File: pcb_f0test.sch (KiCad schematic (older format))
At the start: 36 parts, among them P2 CONN_01X02, P6 CONN_02X05, U1 STM32F042GxU, U2 LP2985LV

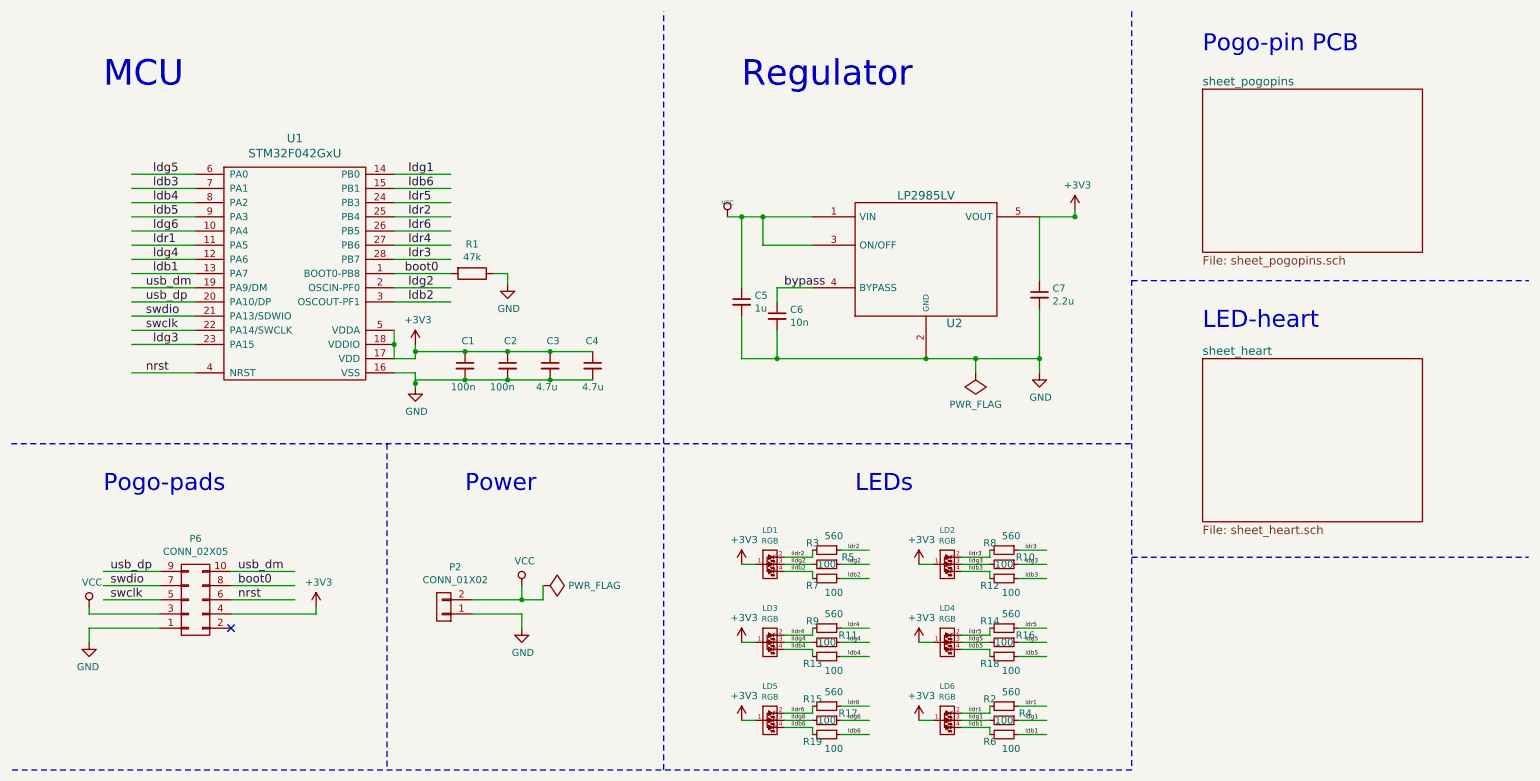
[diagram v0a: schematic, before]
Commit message: Change RGB LED footprint to match new batch of cheap 0603.
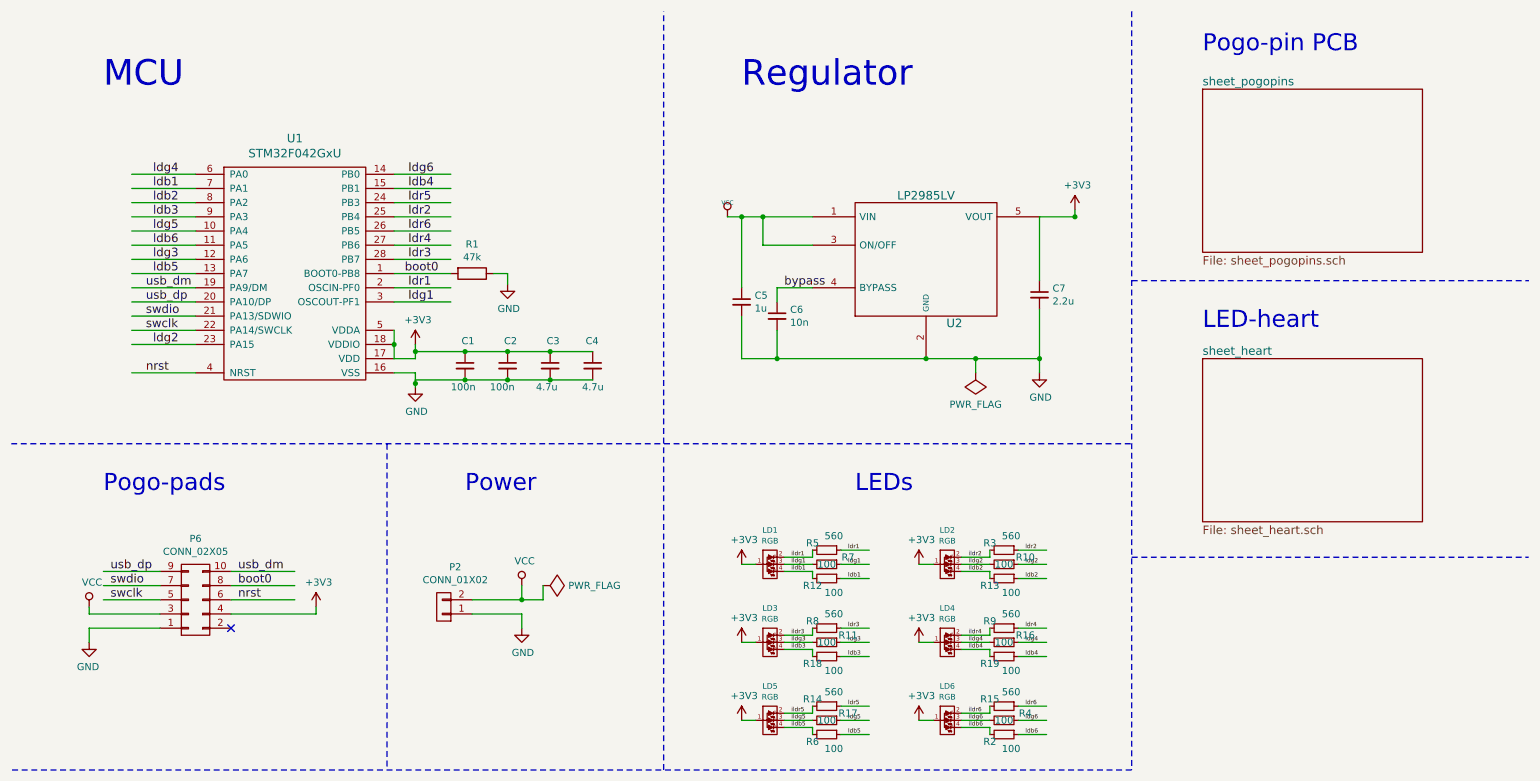
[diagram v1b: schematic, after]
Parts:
- LD1, LD2, LD3, LD4, LD5, LD6: footprint knielsenlib:RGB_0603 -> knielsenlib:RGB_0603_ALTPINOUT
- renumbered R7 to R12, R12 to R13, R15 to R14, R2 to R15, R13 to R18, R18 to R19, R6 to R2, R8 to R3, R3 to R5, R19 to R6, R5 to R7, R9 to R8, R14 to R9
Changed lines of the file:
@@
 F 0 "LD6" H 7100 5741 40  0000 C CNN
 F 1 "RGB" H 7100 5665 40  0000 C CNN
-F 2 "knielsenlib:RGB_0603" H 6575 5575 60  0001 C CNN
+F 2 "knielsenlib:RGB_0603_ALTPINOUT" H 6575 5575 60  0001 C CNN
 F 3 "" H 6575 5575 60  0000 C CNN
 	1    7100 5500
@@
 	7200 5550 7400 5550
 Text Label 7650 5400 0    30   ~ 0
-ldr1
+ldr6
 Text Label 7650 5500 0    30   ~ 0
-ldg1
+ldg6
 Text Label 7650 5600 0    30   ~ 0
-ldb1
-$Comp
-L R_Small R2
+ldb6
+$Comp
+L R_Small R15
 U 1 1 57548D10
 P 7500 5400
-F 0 "R2" V 7450 5300 50  0000 C CNN
+F 0 "R15" V 7450 5300 50  0000 C CNN
 F 1 "560" V 7400 5450 50  0000 C CNN
 F 2 "Resistors_SMD:R_0603" H 7500 5400 50  0001 C CNN
@@
 $EndComp
 $Comp
-L R_Small R6
+L R_Small R2
 U 1 1 57548DC6
 P 7500 5600
-F 0 "R6" V 7550 5500 50  0000 C CNN
+F 0 "R2" V 7550 5500 50  0000 C CNN
 F 1 "100" V 7600 5650 50  0000 C CNN
 F 2 "Resistors_SMD:R_0603" H 7500 5600 50  0001 C CNN
@@
 	7600 5600 7800 5600
 Text Label 7250 5450 0    30   ~ 0
-ildr1
+ildr6
 Text Label 7250 5500 0    30   ~ 0
-ildg1
+ildg6
 Text Label 7250 5550 0    30   ~ 0
-ildb1
+ildb6
 $Comp
 L RGB_LED_SMALL LD1
@@
 F 0 "LD1" H 5850 4641 40  0000 C CNN
 F 1 "RGB" H 5850 4565 40  0000 C CNN
-F 2 "knielsenlib:RGB_0603" H 5325 4475 60  0001 C CNN
+F 2 "knielsenlib:RGB_0603_ALTPINOUT" H 5325 4475 60  0001 C CNN
 F 3 "" H 5325 4475 60  0000 C CNN
 	1    5850 4400
@@
 	5950 4450 6150 4450
 Text Label 6400 4300 0    30   ~ 0
-ldr2
+ldr1
 Text Label 6400 4400 0    30   ~ 0
-ldg2
+ldg1
 Text Label 6400 4500 0    30   ~ 0
-ldb2
-$Comp
-L R_Small R3
+ldb1
+$Comp
+L R_Small R5
 U 1 1 57549926
 P 6250 4300
-F 0 "R3" V 6200 4200 50  0000 C CNN
+F 0 "R5" V 6200 4200 50  0000 C CNN
 F 1 "560" V 6150 4350 50  0000 C CNN
 F 2 "Resistors_SMD:R_0603" H 6250 4300 50  0001 C CNN
@@
 $EndComp
 $Comp
-L R_Small R5
+L R_Small R7
 U 1 1 5754992C
 P 6250 4400
-F 0 "R5" V 6200 4550 50  0000 C CNN
+F 0 "R7" V 6200 4550 50  0000 C CNN
 F 1 "100" V 6250 4400 50  0000 C CNN
 F 2 "Resistors_SMD:R_0603" H 6250 4400 50  0001 C CNN
@@
 $EndComp
 $Comp
-L R_Small R7
+L R_Small R12
 U 1 1 57549932
 P 6250 4500
-F 0 "R7" V 6300 4400 50  0000 C CNN
+F 0 "R12" V 6300 4400 50  0000 C CNN
 F 1 "100" V 6350 4550 50  0000 C CNN
 F 2 "Resistors_SMD:R_0603" H 6250 4500 50  0001 C CNN
@@
 	6350 4500 6550 4500
 Text Label 6000 4350 0    30   ~ 0
-ildr2
+ildr1
 Text Label 6000 4400 0    30   ~ 0
-ildg2
+ildg1
 Text Label 6000 4450 0    30   ~ 0
-ildb2
+ildb1
 $Comp
 L RGB_LED_SMALL LD2
@@
 F 0 "LD2" H 7100 4641 40  0000 C CNN
 F 1 "RGB" H 7100 4565 40  0000 C CNN
-F 2 "knielsenlib:RGB_0603" H 6575 4475 60  0001 C CNN
+F 2 "knielsenlib:RGB_0603_ALTPINOUT" H 6575 4475 60  0001 C CNN
 F 3 "" H 6575 4475 60  0000 C CNN
 	1    7100 4400
@@
 	7200 4450 7400 4450
 Text Label 7650 4300 0    30   ~ 0
-ldr3
+ldr2
 Text Label 7650 4400 0    30   ~ 0
-ldg3
+ldg2
 Text Label 7650 4500 0    30   ~ 0
-ldb3
-$Comp
-L R_Small R8
+ldb2
+$Comp
+L R_Small R3
 U 1 1 57549ECC
 P 7500 4300
-F 0 "R8" V 7450 4200 50  0000 C CNN
+F 0 "R3" V 7450 4200 50  0000 C CNN
 F 1 "560" V 7400 4350 50  0000 C CNN
 F 2 "Resistors_SMD:R_0603" H 7500 4300 50  0001 C CNN
@@
 $EndComp
 $Comp
-L R_Small R12
+L R_Small R13
 U 1 1 57549EDA
 P 7500 4500
-F 0 "R12" V 7550 4400 50  0000 C CNN
+F 0 "R13" V 7550 4400 50  0000 C CNN
 F 1 "100" V 7600 4550 50  0000 C CNN
 F 2 "Resistors_SMD:R_0603" H 7500 4500 50  0001 C CNN
@@
 	7600 4500 7800 4500
 Text Label 7250 4350 0    30   ~ 0
-ildr3
+ildr2
 Text Label 7250 4400 0    30   ~ 0
-ildg3
+ildg2
 Text Label 7250 4450 0    30   ~ 0
-ildb3
+ildb2
 $Comp
 L RGB_LED_SMALL LD3
@@
 F 0 "LD3" H 5850 5191 40  0000 C CNN
 F 1 "RGB" H 5850 5115 40  0000 C CNN
-F 2 "knielsenlib:RGB_0603" H 5325 5025 60  0001 C CNN
+F 2 "knielsenlib:RGB_0603_ALTPINOUT" H 5325 5025 60  0001 C CNN
 F 3 "" H 5325 5025 60  0000 C CNN
 	1    5850 4950
@@
 	5950 5000 6150 5000
 Text Label 6400 4850 0    30   ~ 0
-ldr4
+ldr3
 Text Label 6400 4950 0    30   ~ 0
-ldg4
+ldg3
 Text Label 6400 5050 0    30   ~ 0
-ldb4
-$Comp
-L R_Small R9
+ldb3
+$Comp
+L R_Small R8
 U 1 1 57549EFD
 P 6250 4850
-F 0 "R9" V 6200 4750 50  0000 C CNN
+F 0 "R8" V 6200 4750 50  0000 C CNN
 F 1 "560" V 6150 4900 50  0000 C CNN
 F 2 "Resistors_SMD:R_0603" H 6250 4850 50  0001 C CNN
@@
 $EndComp
 $Comp
-L R_Small R13
+L R_Small R18
 U 1 1 57549F0B
 P 6250 5050
-F 0 "R13" V 6300 4950 50  0000 C CNN
+F 0 "R18" V 6300 4950 50  0000 C CNN
 F 1 "100" V 6350 5100 50  0000 C CNN
 F 2 "Resistors_SMD:R_0603" H 6250 5050 50  0001 C CNN
@@
 	6350 5050 6550 5050
 Text Label 6000 4900 0    30   ~ 0
-ildr4
+ildr3
 Text Label 6000 4950 0    30   ~ 0
-ildg4
+ildg3
 Text Label 6000 5000 0    30   ~ 0
-ildb4
+ildb3
 $Comp
 L RGB_LED_SMALL LD4
@@
 F 0 "LD4" H 7100 5191 40  0000 C CNN
 F 1 "RGB" H 7100 5115 40  0000 C CNN
-F 2 "knielsenlib:RGB_0603" H 6575 5025 60  0001 C CNN
+F 2 "knielsenlib:RGB_0603_ALTPINOUT" H 6575 5025 60  0001 C CNN
 F 3 "" H 6575 5025 60  0000 C CNN
 	1    7100 4950
@@
 	7200 5000 7400 5000
 Text Label 7650 4850 0    30   ~ 0
-ldr5
+ldr4
 Text Label 7650 4950 0    30   ~ 0
-ldg5
+ldg4
 Text Label 7650 5050 0    30   ~ 0
-ldb5
-$Comp
-L R_Small R14
+ldb4
+$Comp
+L R_Small R9
 U 1 1 5754A28A
 P 7500 4850
-F 0 "R14" V 7450 4750 50  0000 C CNN
+F 0 "R9" V 7450 4750 50  0000 C CNN
 F 1 "560" V 7400 4900 50  0000 C CNN
 F 2 "Resistors_SMD:R_0603" H 7500 4850 50  0001 C CNN
@@
 $EndComp
 $Comp
-L R_Small R18
+L R_Small R19
 U 1 1 5754A298
 P 7500 5050
-F 0 "R18" V 7550 4950 50  0000 C CNN
+F 0 "R19" V 7550 4950 50  0000 C CNN
 F 1 "100" V 7600 5100 50  0000 C CNN
 F 2 "Resistors_SMD:R_0603" H 7500 5050 50  0001 C CNN
@@
 	7600 5050 7800 5050
 Text Label 7250 4900 0    30   ~ 0
-ildr5
+ildr4
 Text Label 7250 4950 0    30   ~ 0
-ildg5
+ildg4
 Text Label 7250 5000 0    30   ~ 0
-ildb5
+ildb4
 $Comp
 L RGB_LED_SMALL LD5
@@
 F 0 "LD5" H 5850 5741 40  0000 C CNN
 F 1 "RGB" H 5850 5665 40  0000 C CNN
-F 2 "knielsenlib:RGB_0603" H 5325 5575 60  0001 C CNN
+F 2 "knielsenlib:RGB_0603_ALTPINOUT" H 5325 5575 60  0001 C CNN
 F 3 "" H 5325 5575 60  0000 C CNN
 	1    5850 5500
@@
 	5950 5550 6150 5550
 Text Label 6400 5400 0    30   ~ 0
-ldr6
+ldr5
 Text Label 6400 5500 0    30   ~ 0
-ldg6
+ldg5
 Text Label 6400 5600 0    30   ~ 0
-ldb6
-$Comp
-L R_Small R15
+ldb5
+$Comp
+L R_Small R14
 U 1 1 5754A2BB
 P 6250 5400
-F 0 "R15" V 6200 5300 50  0000 C CNN
+F 0 "R14" V 6200 5300 50  0000 C CNN
 F 1 "560" V 6150 5450 50  0000 C CNN
 F 2 "Resistors_SMD:R_0603" H 6250 5400 50  0001 C CNN
@@
 $EndComp
 $Comp
-L R_Small R19
+L R_Small R6
 U 1 1 5754A2C9
 P 6250 5600
-F 0 "R19" V 6300 5500 50  0000 C CNN
+F 0 "R6" V 6300 5500 50  0000 C CNN
 F 1 "100" V 6350 5650 50  0000 C CNN
 F 2 "Resistors_SMD:R_0603" H 6250 5600 50  0001 C CNN
@@
 	6350 5600 6550 5600
 Text Label 6000 5450 0    30   ~ 0
-ildr6
+ildr5
 Text Label 6000 5500 0    30   ~ 0
-ildg6
+ildg5
 Text Label 6000 5550 0    30   ~ 0
-ildb6
+ildb5
 Wire Wire Line
 	1800 1650 1350 1650
@@
 	3200 2550 3600 2550
 Text Label 1500 2150 0    60   ~ 0
-ldr1
+ldb6
 Text Label 3300 1650 0    60   ~ 0
-ldg1
+ldg6
 Text Label 1500 2350 0    60   ~ 0
-ldb1
+ldb5
 Text Label 3300 1950 0    60   ~ 0
 ldr2
 Text Label 3300 2450 0    60   ~ 0
-ldg2
+ldr1
 Text Label 3300 2550 0    60   ~ 0
-ldb2
+ldg1
 Text Label 3300 2250 0    60   ~ 0
 ldr3
 Text Label 1500 2850 0    60   ~ 0
-ldg3
+ldg2
 Text Label 1500 1750 0    60   ~ 0
-ldb3
+ldb1
 Text Label 3300 2150 0    60   ~ 0
 ldr4
 Text Label 1500 2250 0    60   ~ 0
-ldg4
+ldg3
 Text Label 1500 1850 0    60   ~ 0
-ldb4
+ldb2
 Text Label 3300 1850 0    60   ~ 0
 ldr5
 Text Label 1500 1650 0    60   ~ 0
-ldg5
+ldg4
 Text Label 1500 1950 0    60   ~ 0
-ldb5
+ldb3
 Text Label 3300 2050 0    60   ~ 0
 ldr6
 Text Label 1500 2050 0    60   ~ 0
-ldg6
+ldg5
 Text Label 3300 1750 0    60   ~ 0
-ldb6
+ldb4
 $Sheet
 S 8900 1050 1550 1150
